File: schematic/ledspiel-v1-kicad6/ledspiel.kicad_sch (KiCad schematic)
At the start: 101 parts, among them J1 Conn_Battery, J3 USART Debug, J3 USB_B_Micro, J4 Micro_SD_Card, Q10 BSS138, Q11 BSS138, Q12 BSS138, Q13 BSS138, Q14 BSS138, Q40 IRLML6402, U1 STM32F405RGTx, U2 USBLC6-2SC6, U3 MCP1640CH, Y1 8MHz, Y2 32768Hz

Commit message: WIP schematic
footprints for LEDs
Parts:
- removed JP2: SolderJumper_3_Open, symbol Jumper:SolderJumper_3_Open
- added C20, C21, C60: 2.2µF, symbol Device:C
- added D3: DO-214AC, symbol Device:D_Schottky
- added Q60: SFH300-3/4, symbol Device:Q_Photo_NPN
- added R50: 68Ω, symbol Device:R
- added R60: 180Ω, symbol Device:R
- added R61: 976kΩ, symbol Device:R
- added R62: 1kΩ, symbol Device:R
- added R63: 56kΩ, symbol Device:R
- added U4: LP38693MP-3.3, Package_TO_SOT_SMD:SOT-223-5, symbol Regulator_Linear:LP38693MP-3.3
- added U6: TSOP312xx, OptoDevice:Vishay_CAST-3Pin, symbol Interface_Optical:TSOP312xx
- D1: value D_Schottky -> DO-214AC
- D10, D11, D12, D13, D14, D20, D21, D22, D23, D25, D30, D31, D32, D33, D34, D40, D41, D42, D43, D44, D50, D51, D52, D53, D54: footprint (none) -> LED_THT:LED_D5.0mm-4_RGB
- F1: value 250mA -> 500mA
- R41: value 200Ω -> 180Ω
- renumbered C3 to C2, C2 to C3, J3 to J5, JP3 to JP2, R5 to R1, R3 to R2, R4 to R3, R1 to R4, R2 to R5, R7 to R6, R6 to R7
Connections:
- net +3.3V: now also R61.1
- net GND: now also C20.2, C21.2, C60.2, Q60.2 (E), U4.5 (GND), U6.1 (GND); no longer C5.2
- net GNDA: now also C5.2
- net Vin: now also U1.1 (VBAT), R50.2
- net at J5.1 (VBUS): now also C20.1, U4.1 (EN), U4.4 (IN)
- net LightIn: now reaches U1.14 (PA0)
- net LightIn: now also Q60.1 (C), R61.2, R62.2, R63.2
- net LightOut1: now reaches U1.15 (PA1)
- net LightOut1: now also R63.1
- net LightOut2: now reaches U1.16 (PA2)
- net LightOut2: now also R62.1
- net at U1.52 (PC11): now also R60.2
- net at U1.53 (PC12): now also U6.3 (OUT)
- new net: C60.1, R60.1, U6.2 (Vs)
- new net: C21.1, D3.2 (A), U4.3 (OUT)
- new net: D3.1 (K), R50.1
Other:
- note added: "C/85 startup charger at 8.8mA"
- note added: "Resonance of L2 + C5 F=50.32kHz"
- note added: "Vin: 1.2V...3V best are 2x NIMH batteries 750mAh"
- note removed: "Resonance F=50.32kHz"
- note removed: "Vin: 1.2V...3V best are 2x NIMH batteries"
- moved on the sheet: C3, C4, C5, C6, J5, JP1, L1, L2, LS1, R2, R3, R4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

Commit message: WIP
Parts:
- added D4: LED, symbol Device:LED
- added J50: Conn_01x16_Male, symbol Connector:Conn_01x16_Male
- added Q1: BSS138, Package_TO_SOT_SMD:SOT-23, symbol Transistor_FET:BSS138
- added R51, R52, R53, R54, R55, R56, R57: 180Ω, symbol Device:R
- added R58, R59, R8: 330kΩ, symbol Device:R
- added R7: 100kΩ, symbol Device:R
- added TP1, TP2, TP3, TP4, TP5, TP6, TP60: TestPoint, symbol Connector:TestPoint
- R50: value 68Ω -> 180Ω
- renumbered R7 to R9
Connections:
- net +3.3V: now also J50.10 (Pin_10), J50.12 (Pin_12), J50.14 (Pin_14), J50.16 (Pin_16), J50.2 (Pin_2), J50.4 (Pin_4), J50.6 (Pin_6), J50.8 (Pin_8), TP3.1
- net Boot1: now also R57.1, R59.1
- net GND: now also Q1.2 (S), R58.2, R59.2, R7.2, R8.1, TP5.1
- net GNDA: now also TP6.1
- net LightIn: now also TP60.1
- net VDDA: now also TP4.1
- net Vin: now also D3.1 (K), TP2.1; no longer R50.2
- net at C2.2, R2.2, R3.1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: now also Q1.3 (D)
- net at F1.1, J1.1 (Pin_1): now also TP1.1
- net at C21.1, D3.2 (A), U4.3 (OUT): now also D4.2 (A)
- net at R50.1: now also U1.54 (PD2), U1.60 (BOOT0), R58.1; no longer D3.1 (K)
- net at U1.2 (PC13): now also R56.1
- net at U1.37 (PC6): now also R51.1
- net at U1.38 (PC7): now also R52.1
- net at U1.39 (PC8): now also R53.1
- net at U1.40 (PC9): now also R54.1
- net PowerOff: now reaches U1.50 (PA15)
- net PowerOff: now also Q1.1 (G), R8.2
- net at U1.51 (PC10): now also R55.1
- new net: J50.1 (Pin_1), R50.2
- new net: J50.11 (Pin_11), R55.2
- new net: J50.13 (Pin_13), R56.2
- new net: J50.15 (Pin_15), R57.2
- new net: J50.3 (Pin_3), R51.2
- new net: J50.5 (Pin_5), R52.2
- new net: J50.7 (Pin_7), R53.2
- new net: J50.9 (Pin_9), R54.2
- new net: D4.1 (K), R7.1
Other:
- note added: "BOOT0 must be low for a normal program start high for going to the bootloader"
- note added: "SWCLK"
- note added: "SWDIO"
- note added: "USART BOOT RX"
- note added: "USART BOOT TX"
- note removed: "C/85 startup charger at 8.8mA"
- moved on the sheet: C10, C12, C15, C16, C20, C21, C60, C7, C8, C9, D3, LS1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

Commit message: WIP: Add LM
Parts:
- removed J4: Micro_SD_Card, symbol Connector:Micro_SD_Card
- added J4: SWD Debug, symbol Connector:Conn_01x04_Female
- added J4: Micro_SD_Card_Det, symbol Connector:Micro_SD_Card_Det
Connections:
- net GND: now also J4.2 (Pin_2), J4.6 (VSS)
- net SdCs: now also J4.2 (DAT3/CD)
- net Spi1Miso: now also J4.7 (DAT0)
- net Spi1Mosi: now also J4.3 (CMD)
- net Spi1Sck: now also J4.5 (CLK)
- net Swdio: now reaches U1.46 (PA13)
- net Swdio: now also J4.3 (Pin_3)
- net Swdclk: now reaches U1.49 (PA14)
- net Swdclk: now also J4.1 (Pin_1)
- net at R42.1: now also J4.8 (DAT1)
- net at C40.1, Q40.3 (D), R42.2: now also J4.4 (VDD)
- net at JP4.1 (A): now also J4.11 (SHIELD)
- no-connect marks 2 -> 4
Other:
- note removed: "SWCLK"
- note removed: "SWDIO"
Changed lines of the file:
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@@
   (junction (at 67.31 55.88) (diameter 0) (color 0 0 0 0)
   )
+  (no_connect (at 157.48 250.19))
   (no_connect (at 173.99 78.74))
   (no_connect (at 157.48 229.87))
+  (no_connect (at 157.48 252.73))
   (wire (pts (xy 299.72 77.47) (xy 299.72 102.87))
     (stroke (width 0) (type default) (color 0 0 0 0))
@@
     (stroke (width 0) (type default) (color 0 0 0 0))
   )
-  (wire (pts (xy 121.92 138.43) (xy 135.89 138.43))
+  (wire (pts (xy 121.92 138.43) (xy 189.23 138.43))
     (stroke (width 0) (type default) (color 0 0 0 0))
   )
@@
     (stroke (width 0) (type default) (color 0 0 0 0))
   )
+  (wire (pts (xy 189.23 124.46) (xy 189.23 138.43))
+    (stroke (width 0) (type default) (color 0 0 0 0))
+  )
   (wire (pts (xy 297.18 107.95) (xy 297.18 133.35))
     (stroke (width 0) (type default) (color 0 0 0 0))
@@
     (stroke (width 0) (type default) (color 0 0 0 0))
   )
+  (wire (pts (xy 184.15 124.46) (xy 184.15 140.97))
+    (stroke (width 0) (type default) (color 0 0 0 0))
+  )
   (wire (pts (xy 121.92 184.15) (xy 139.7 184.15))
     (stroke (width 0) (type default) (color 0 0 0 0))
@@
     (stroke (width 0) (type default) (color 0 0 0 0))
   )
+  (wire (pts (xy 186.69 124.46) (xy 186.69 127))
+    (stroke (width 0) (type default) (color 0 0 0 0))
+  )
   (wire (pts (xy 67.31 44.45) (xy 67.31 45.72))
     (stroke (width 0) (type default) (color 0 0 0 0))
@@
     (stroke (width 0) (type default) (color 0 0 0 0))
   )
-  (wire (pts (xy 121.92 140.97) (xy 135.89 140.97))
+  (wire (pts (xy 121.92 140.97) (xy 184.15 140.97))
     (stroke (width 0) (type default) (color 0 0 0 0))
   )
@@
     (stroke (width 0) (type default) (color 0 0 0 0))
   )
+  (wire (pts (xy 157.48 252.73) (xy 160.02 252.73))
+    (stroke (width 0) (type default) (color 0 0 0 0))
+  )
   (wire (pts (xy 290.83 52.07) (xy 299.72 52.07))
     (stroke (width 0) (type default) (color 0 0 0 0))
@@
     (stroke (width 0) (type default) (color 0 0 0 0))
   )
+  (wire (pts (xy 157.48 250.19) (xy 160.02 250.19))
+    (stroke (width 0) (type default) (color 0 0 0 0))
+  )
   (wire (pts (xy 151.13 86.36) (xy 151.13 83.82))
     (stroke (width 0) (type default) (color 0 0 0 0))
@@
     (effects (font (size 1.27 1.27)) (justify left bottom))
   )
-  (text "SWCLK" (at 129.54 140.97 0)
-    (effects (font (size 1.27 1.27)) (justify left bottom))
-  )
-  (text "SWDIO" (at 129.54 138.43 0)
-    (effects (font (size 1.27 1.27)) (justify left bottom))
-  )
   (label "Line5" (at 241.3 149.86 0)
     (effects (font (size 1.27 1.27)) (justify left bottom))
@@
     (effects (font (size 1.27 1.27)) (justify left bottom))
   )
+  (label "Swdio" (at 121.92 138.43 0)
+    (effects (font (size 1.27 1.27)) (justify left bottom))
+  )
+  (label "Swdclk" (at 121.92 140.97 0)
+    (effects (font (size 1.27 1.27)) (justify left bottom))
+  )
   (label "Line5" (at 81.28 158.75 0)
     (effects (font (size 1.27 1.27)) (justify left bottom))
@@
     (effects (font (size 1.27 1.27)) (justify left bottom))
   )
-  (label "PowerOff" (at 123.19 143.51 0)
+  (label "PowerOff" (at 121.92 143.51 0)
     (effects (font (size 1.27 1.27)) (justify left bottom))
   )
@@
     (pin "1")
   )
+  (symbol (lib_id "Connector:Conn_01x04_Female") (at 186.69 119.38 90) (unit 1)
+    (in_bom yes) (on_board yes) (fields_autoplaced)
+    (property "Reference" "J4" (id 0) (at 187.96 114.3 90))
+    (property "Value" "SWD Debug" (id 1) (at 187.96 116.84 90))
+    (property "Footprint" "" (id 2) (at 186.69 119.38 0)
+      (effects (font (size 1.27 1.27)) hide)
+    )
+    (property "Datasheet" "~" (id 3) (at 186.69 119.38 0)
+      (effects (font (size 1.27 1.27)) hide)
+    )
+    (pin "1")
+    (pin "2")
+    (pin "3")
+    (pin "4")
+  )
   (symbol (lib_id "power:GND") (at 146.05 242.57 0) (unit 1)
     (in_bom yes) (on_board yes) (fields_autoplaced)
@@
     (pin "3")
   )
-  (symbol (lib_id "Connector:Micro_SD_Card") (at 182.88 237.49 0) (unit 1)
-    (in_bom yes) (on_board yes) (fields_autoplaced)
-    (property "Reference" "J4" (id 0) (at 183.515 219.8202 0))
-    (property "Value" "Micro_SD_Card" (id 1) (at 183.515 222.3571 0))
-    (property "Footprint" "" (id 2) (at 212.09 229.87 0)
-      (effects (font (size 1.27 1.27)) hide)
-    )
-    (property "Datasheet" "http://katalog.we-online.de/em/datasheet/693072010801.pdf" (id 3) (at 182.88 237.49 0)
-      (effects (font (size 1.27 1.27)) hide)
-    )
-    (pin "1")
-    (pin "2")
-    (pin "3")
-    (pin "4")
-    (pin "5")
-    (pin "6")
-    (pin "7")
-    (pin "8")
-    (pin "9")
-  )
   (symbol (lib_id "Device:LED_RKGB") (at 285.75 133.35 0) (unit 1)
     (in_bom yes) (on_board yes) (fields_autoplaced)
@@
     (pin "1")
   )
+  (symbol (lib_id "Connector:Micro_SD_Card_Det") (at 182.88 240.03 0) (unit 1)
+    (in_bom yes) (on_board yes) (fields_autoplaced)
+    (property "Reference" "J4" (id 0) (at 183.515 218.44 0))
+    (property "Value" "Micro_SD_Card_Det" (id 1) (at 183.515 220.98 0))
+    (property "Footprint" "" (id 2) (at 234.95 222.25 0)
+      (effects (font (size 1.27 1.27)) hide)
+    )
+    (property "Datasheet" "https://www.hirose.com/product/en/download_file/key_name/DM3/category/Catalog/doc_file_id/49662/?file_category_id=4&item_id=195&is_series=1" (id 3) (at 182.88 237.49 0)
+      (effects (font (size 1.27 1.27)) hide)
+    )
+    (pin "1")
+    (pin "10")
+    (pin "11")
+    (pin "2")
+    (pin "3")
+    (pin "4")
+    (pin "5")
+    (pin "6")
+    (pin "7")
+    (pin "8")
+    (pin "9")
+  )
   (symbol (lib_id "power:GND") (at 265.43 132.08 0) (unit 1)
     (in_bom yes) (on_board yes)
@@
     (pin "2")
   )
+  (symbol (lib_id "power:GND") (at 186.69 127 0) (unit 1)
+    (in_bom yes) (on_board yes) (fields_autoplaced)
+    (property "Reference" "#PWR?" (id 0) (at 186.69 133.35 0)
+      (effects (font (size 1.27 1.27)) hide)
+    )
+    (property "Value" "GND" (id 1) (at 186.69 131.4434 0))
+    (property "Footprint" "" (id 2) (at 186.69 127 0)
+      (effects (font (size 1.27 1.27)) hide)
+    )
+    (property "Datasheet" "" (id 3) (at 186.69 127 0)
+      (effects (font (size 1.27 1.27)) hide)
+    )
+    (pin "1")
+  )
   (symbol (lib_id "Power_Protection:USBLC6-2SC6") (at 166.37 109.22 0) (unit 1)
     (in_bom yes) (on_board yes) (fields_autoplaced)
@@
       (reference "#PWR0145") (unit 1) (value "GND") (footprint "")
     )
+    (path "/cdbf996f-f703-47a9-b942-793d49c769fa"
+      (reference "#PWR?") (unit 1) (value "GND") (footprint "")
+    )
     (path "/315ec405-f84d-41f5-b6ee-59d298dca57a"
       (reference "C1") (unit 1) (value "10µF") (footprint "")
@@
       (reference "J3") (unit 1) (value "USART Debug") (footprint "")
     )
-    (path "/b10fb92a-abe2-4cf8-8650-b7aa5f625383"
-      (reference "J4") (unit 1) (value "Micro_SD_Card") (footprint "")
+    (path "/70c16904-7537-4c0a-b3a3-fa64963865fb"
+      (reference "J4") (unit 1) (value "SWD Debug") (footprint "")
+    )
+    (path "/bb0243ca-9a80-4200-9d6a-0017ad774b60"
+      (reference "J4") (unit 1) (value "Micro_SD_Card_Det") (footprint "Connector_Card:microSD_HC_Hirose_DM3D-SF")
     )
     (path "/145f17d5-7130-4b50-b488-eb854900bf1f"

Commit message: WIP
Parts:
- removed JP4: SolderJumper_2_Open, symbol Jumper:SolderJumper_2_Open
- added C100: 100nF, symbol Device:C
- added C101, C102: 2.2µF, symbol Device:C
- added C103: 18nF, symbol Device:C
- added JP100: SolderJumper_3_Open, symbol Jumper:SolderJumper_3_Open
- added R100: 330kΩ, symbol Device:R
- added R101: 56kΩ, symbol Device:R
- added R102: 200Ω, symbol Device:R
- added R73, R74, R75: 47Ω, symbol Device:R
- added RV100: 25kΩ, symbol Device:R_Potentiometer
- added U100: LM4861, Package_SO:SOIC-8-N7_3.9x4.9mm_P1.27mm, symbol malteLib2025:LM4861
- C70: renamed from C40; value 100nF -> 2.2µF
- J70: renamed from J4; footprint (none) -> Connector_Card:microSD_HC_Hirose_DM3D-SF
- R50, R51, R52, R53, R54, R55, R56, R57, R60: value 180Ω -> 200Ω
- R70: renamed from R41; value 180Ω -> 200Ω
- R71: renamed from R40; value 562kΩ -> 330kΩ
- R9: value 10kΩ -> 100kΩ
- renumbered JP2 to JP101, LS1 to LS100, Q40 to Q70, R42 to R72, U6 to U60
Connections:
- net Dac1: now also JP101.3 (B), JP100.3 (B); no longer JP101.1 (A)
- net GND: now also J70.11 (SHIELD)
- net GNDA: now also C100.2, C101.2, C103.2, U100.7 (GND)
- net Spi1Miso: now also R75.1; no longer J70.7 (DAT0)
- net Spi1Mosi: now also R73.1; no longer J70.3 (CMD)
- net Spi1Sck: now also R74.1; no longer J70.5 (CLK)
- net Tim2Ch4: now also JP101.1 (A), JP100.1 (A); no longer JP101.3 (B)
- net VDDA: now also C100.1, R100.2, U100.6 (VDD)
- net at R9.1, U1.7 (NRST): now also J4.4 (Pin_4)
- net at JP101.2 (C): now also R102.1
- net at LS100.1: now also RV100.2, U100.5 (Vo1)
- net at LS100.2: now also U100.8 (Vo2)
- new net: JP100.2 (C), R100.1, U100.1 (SHDN)
- new net: C101.1, U100.2 (BYPASS), U100.3 (IN+)
- new net: R101.2, U100.4 (IN-)
- new net: J70.5 (CLK), R74.2
- new net: C102.2, R101.1, RV100.3
- new net: C102.1, C103.1, R102.2
- new net: J70.3 (CMD), R73.2
- new net: J70.7 (DAT0), R75.2
- no-connect marks 4 -> 5
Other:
- note added: "C103 only if PWM is used"
- note added: "Namings: 0...9: STM32 + I/O + USB 10...59: LED Matrix 60...69: Brightness and IR input 70...79: SD card 80...99: Power supply 100...109: Sound"
- note added: "One pin of the STM provides audio data the other controls the shutdown"
- note added: "maximum gain: 0.89"
- moved on the sheet: C10, C11, C12, C13, C14, C15, C16, C60, C7, C70, C8, C9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

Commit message: WIP
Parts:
- removed JP1: SolderJumper_2_Open, symbol Jumper:SolderJumper_2_Open
- added J5: USB_C_Receptacle_USB2.0, symbol Connector:USB_C_Receptacle_USB2.0
- added R2, R3: 5.1kΩ, symbol Device:R
- renumbered C13 to C1, C14 to C2, C16 to C3, C15 to C4, C1 to C80, C2 to C81, C3 to C82, C4 to C83, C5 to C84, C6 to C85, C20 to C86, C21 to C87, C7 to C88, C8 to C89, C9 to C90, C10 to C91, C11 to C92, C12 to C93, D1 to D80, D2 to D81, D3 to D82, D4 to D83, F1 to F80, J50 to J1, J4 to J2, J5 to J4, J1 to J80, Q1 to Q80, R9 to R1, R50 to R110, R51 to R111, R52 to R112, R53 to R113, R54 to R114, R55 to R115, R56 to R116, R57 to R117, R58 to R2, R59 to R3, R1 to R80, R2 to R82, R3 to R83, R4 to R84, R5 to R85, R6 to R86, R7 to R87, TP1 to TP80, TP2 to TP81, TP5 to TP82, TP3 to TP83, TP4 to TP84, TP6 to TP85, U3 to U80, U4 to U81
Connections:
- net GND: now also J4.6 (Shield), J5.A1 (GND), J5.A12 (GND), J5.B1 (GND), J5.B12 (GND), J5.S1 (SHIELD), R2.1, R3.1
- net at C86.1, J4.1 (VBUS), U81.1 (EN)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: now also J5.A4 (VBUS), J5.A9 (VBUS), J5.B4 (VBUS), J5.B9 (VBUS)
- net at J4.2 (D-), U2.6 (I/O1): now also J5.A7 (D-), J5.B7 (D-)
- net at J4.3 (D+), U2.4 (I/O2): now also J5.A6 (D+), J5.B6 (D+)
- new net: J5.A5 (CC1), R3.2
- new net: J5.B5 (CC2), R2.2
- no-connect marks 5 -> 7
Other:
- note added: "Namings: 1...9: STM32 + I/O + USB 10...59: LED Matrix 60...69: Brightness and IR input 70...79: SD card 80...99: Power supply 100...109: Sound 110...119: External I/O"
- note added: "Only J4 or J5 may be populated"
- note removed: "Namings: 0...9: STM32 + I/O + USB 10...59: LED Matrix 60...69: Brightness and IR input 70...79: SD card 80...99: Power supply 100...109: Sound"
- moved on the sheet: J4, R100

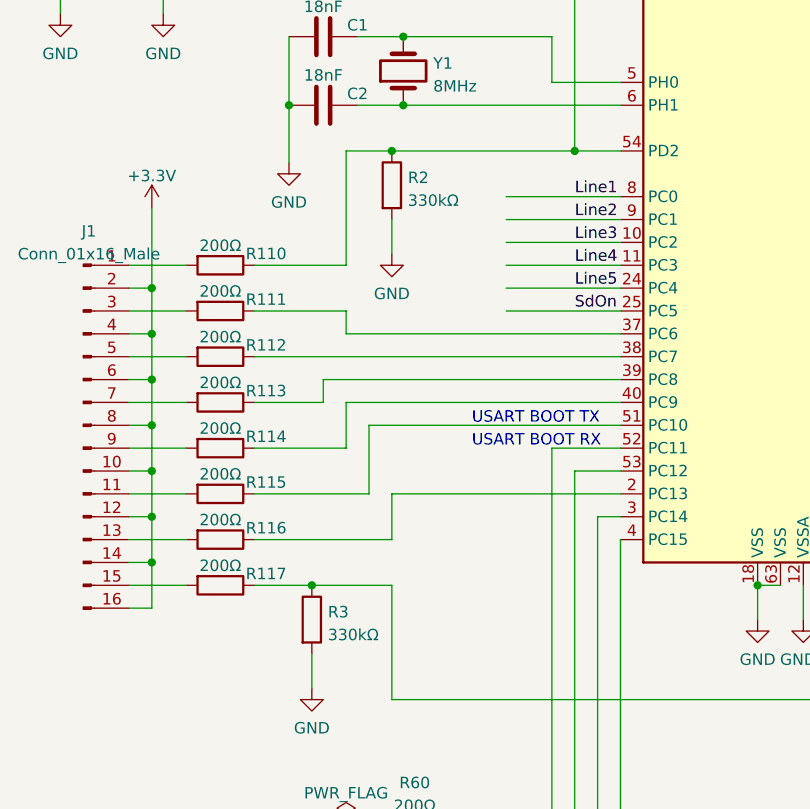
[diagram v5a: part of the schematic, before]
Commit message: WIP: Foodprints mostly
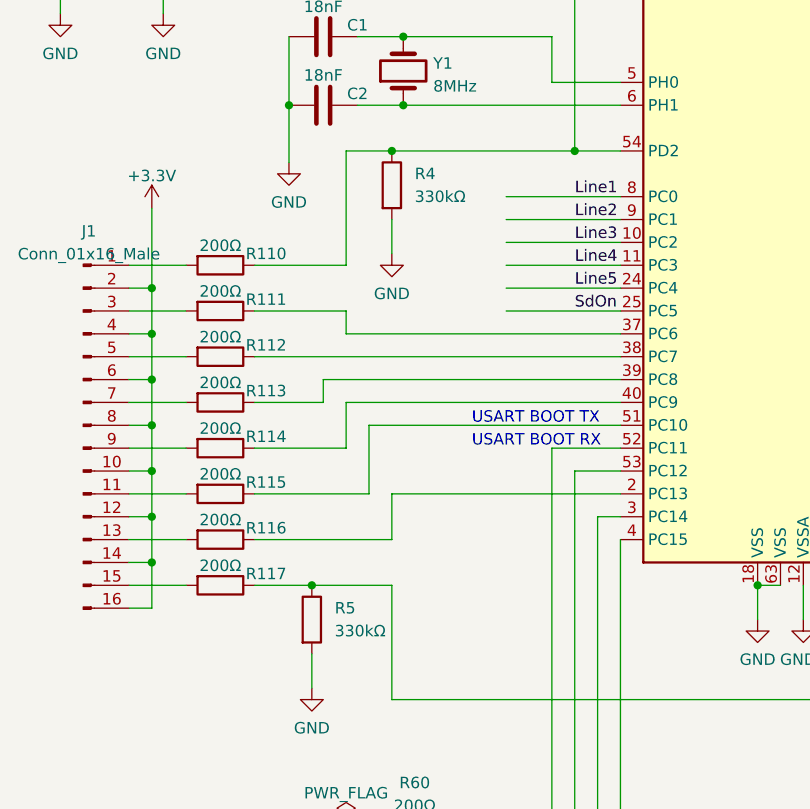
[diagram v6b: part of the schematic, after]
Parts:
- C1, C100, C101, C102, C103, C2, C3, C4, C60, C70, C80, C81, C82, C83, C84, C85, C86, C87, C88, C89, C90, C91, C92, C93: footprint (none) -> Capacitor_SMD:C_0805_2012Metric_Pad1.18x1.45mm_HandSolder
- D81, D83, RV100: footprint (none) -> LED_SMD:LED_0805_2012Metric_Pad1.15x1.40mm_HandSolder
- H1, H2, H3, H4: footprint (none) -> MountingHole:MountingHole_3.2mm_M3_Pad
- J5: footprint (none) -> Connector_USB:USB_C_Receptacle_GCT_USB4085
- JP100, JP101: footprint (none) -> Jumper:SolderJumper-3_P1.3mm_Open_RoundedPad1.0x1.5mm_NumberLabels
- R1, R10, R100, R101, R102, R11, R110, R111, R112, R113, R114, R115, R116, R117, R12, R13, R14, R15, R16, R17, R18, R19, R2, R20, R21, R22, R23, R24, R3, R30, R31, R32, R33, R34, R60, R61, R62, R63, R70, R71, R72, R73, R74, R75, R8, R80, R82, R83, R84, R85, R86, R87: footprint (none) -> Resistor_SMD:R_0805_2012Metric_Pad1.20x1.40mm_HandSolder
- R4: renamed from R2; footprint (none) -> Resistor_SMD:R_0805_2012Metric_Pad1.20x1.40mm_HandSolder
- R5: renamed from R3; footprint (none) -> Resistor_SMD:R_0805_2012Metric_Pad1.20x1.40mm_HandSolder
- TP60: footprint (none) -> TestPoint:TestPoint_Bridge_Pitch2.0mm_Drill0.7mm
- TP80, TP81, TP82, TP83, TP84, TP85: footprint (none) -> TestPoint:TestPoint_THTPad_D1.0mm_Drill0.5mm
